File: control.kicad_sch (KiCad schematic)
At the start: 41 parts, among them J4 Conn_01x05_Pin, J5 Conn_01x03_Pin, J6 Conn_01x03_Pin, Q2 AO3400, Q3 DTC143Z, Q4 DMG1012T, SW2 SW_Push, SW3 SW_SPDT, U6 STM32G031G8Ux

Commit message: Prepeared production files
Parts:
- SW2: LCSC C2837531 -> C398057
- SW3: LCSC C398057 -> C431548
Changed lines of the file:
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@@
 			)
 		)
-		(property "LCSC" "C398057"
+		(property "LCSC" "C431548"
 			(at 260.35 38.1 0)
 			(effects
@@
 			)
 		)
-		(property "LCSC" "C2837531"
+		(property "LCSC" "C398057"
 			(at 204.47 58.42 0)
 			(effects

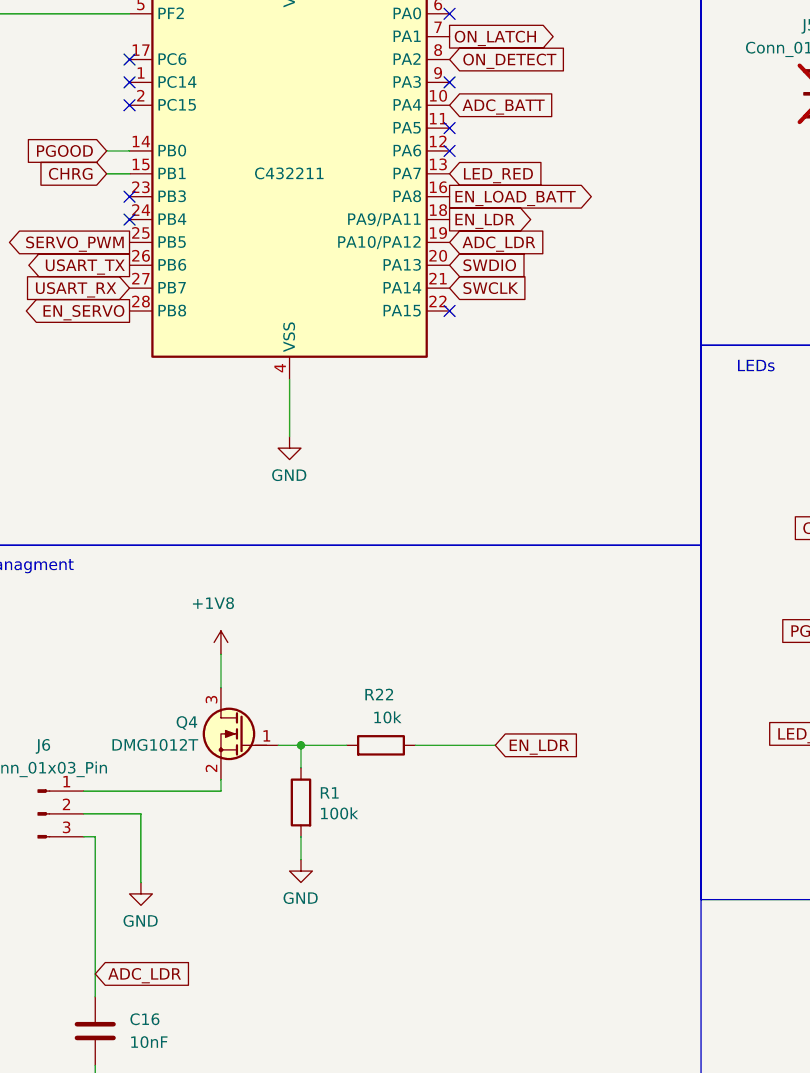
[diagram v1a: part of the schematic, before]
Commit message: Cleaned up libs
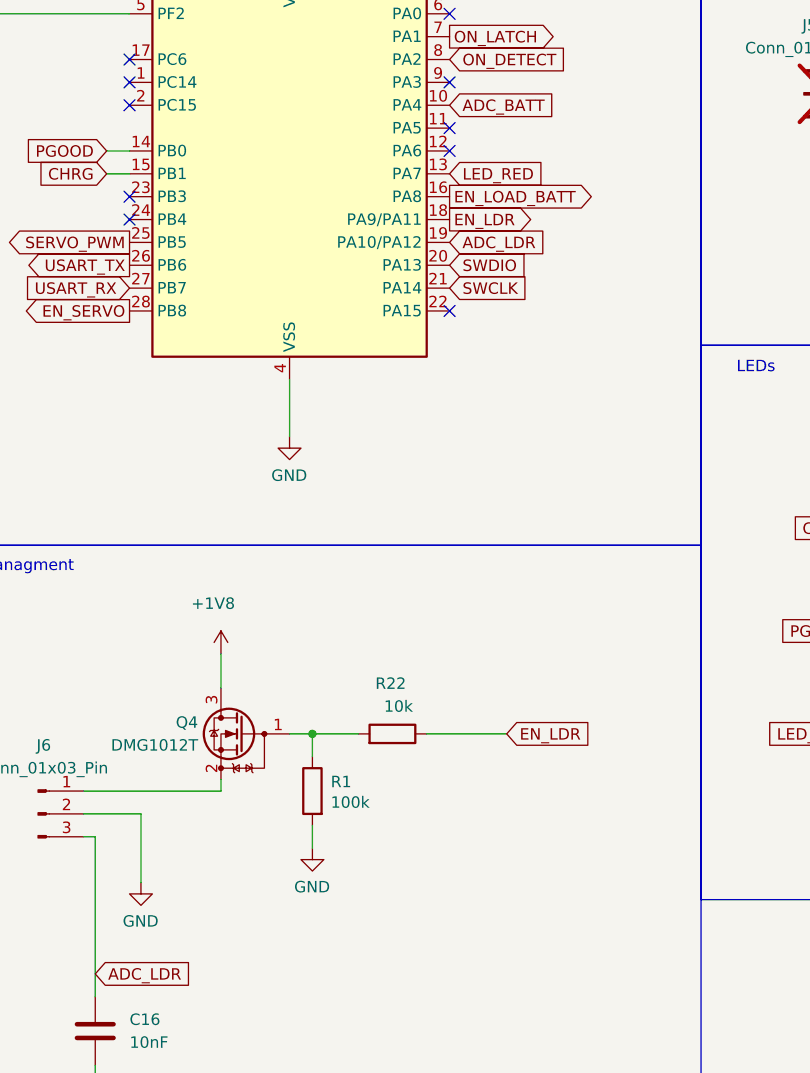
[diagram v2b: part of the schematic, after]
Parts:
- J4: footprint conn:PinHeader_1x05_P1.27mm_Vertical -> Connector_Muffin_THT.pretty:PinHeader_1x05_P1.27mm_Vertical_clear_silk
- J5: footprint conn:PinHeader_1x03_P1.27mm_Vertical -> Connector_Muffin_THT.pretty:PinHeader_1x03_P1.27mm_Vertical_clear_silk
- J6: footprint Muffin_CONNECTOR_THT:Connector_JST_1x03_P1.27mm -> Connector_Muffin_THT.pretty:Connector_JST_1x03_P1.27mm
- Q3: footprint SOT-523:SOT-523 -> Muffin_SMD:SOT-523
- Q4: symbol PCM_Transistor_MOSFET_AKL:DMG1012T -> Transistor_FET:DMG1012T
- U6: symbol stm32g031g8ux:STM32G031G8Ux -> Muffin_MCU:STM32G031G8Ux
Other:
- moved on the sheet: R1, R22
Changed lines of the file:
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@@
 	)
 	(junction
-		(at 85.09 144.78)
+		(at 86.36 143.51)
 		(diameter 0)
 		(color 0 0 0 0)
@@
 	(wire
 		(pts
-			(xy 97.79 144.78) (xy 106.68 144.78)
+			(xy 99.06 143.51) (xy 107.95 143.51)
 		)
 		(stroke
@@
 	(wire
 		(pts
-			(xy 85.09 144.78) (xy 90.17 144.78)
+			(xy 86.36 143.51) (xy 91.44 143.51)
 		)
 		(stroke
@@
 	(wire
 		(pts
-			(xy 85.09 154.94) (xy 85.09 157.48)
+			(xy 86.36 153.67) (xy 86.36 156.21)
 		)
 		(stroke
@@
 	(wire
 		(pts
-			(xy 82.55 144.78) (xy 85.09 144.78)
+			(xy 83.82 143.51) (xy 86.36 143.51)
 		)
 		(stroke
@@
 	(wire
 		(pts
-			(xy 85.09 144.78) (xy 85.09 147.32)
+			(xy 86.36 143.51) (xy 86.36 146.05)
 		)
 		(stroke
@@
 	(global_label "EN_LDR"
 		(shape input)
-		(at 106.68 144.78 0)
+		(at 107.95 143.51 0)
 		(fields_autoplaced yes)
 		(effects
@@
 		)
 		(property "Intersheetrefs" "${INTERSHEET_REFS}"
-			(at 116.6804 144.78 0)
+			(at 117.9504 143.51 0)
 			(effects
 				(font
@@
 			)
 		)
-		(property "Footprint" "conn:PinHeader_1x05_P1.27mm_Vertical"
+		(property "Footprint" "Connector_Muffin_THT.pretty:PinHeader_1x05_P1.27mm_Vertical_clear_silk"
 			(at 139.7 46.99 0)
 			(effects
@@
 	)
 	(symbol
-		(lib_id "PCM_Transistor_MOSFET_AKL:DMG1012T")
+		(lib_id "Transistor_FET:DMG1012T")
 		(at 78.74 143.51 0)
 		(mirror y)
@@
 		)
 		(property "Footprint" "Muffin_SMD:SOT-523"
-			(at 73.66 140.97 0)
+			(at 73.66 145.415 0)
 			(effects
 				(font
 					(size 1.27 1.27)
 				)
+				(justify left)
 				(hide yes)
 			)
 		)
-		(property "Datasheet" "https://www.tme.eu/Document/41ce6a9ee591bb7bae22a8b9f76bcbce/DMG1012T-DTE.pdf"
-			(at 78.74 143.51 0)
+		(property "Datasheet" "https://www.diodes.com/assets/Datasheets/ds31783.pdf"
+			(at 73.66 147.32 0)
 			(effects
 				(font
 					(size 1.27 1.27)
 				)
+				(justify left)
 				(hide yes)
 			)
 		)
-		(property "Description" "SOT-523 N-MOSFET enchancement mode transistor, 20V, 630mA, 280mW, Alternate KiCAD Library"
+		(property "Description" "20V Vds, 0.63 Id, N-Channel MOSFET with ESD protection, SOT-523"
 			(at 78.74 143.51 0)
 			(effects
@@
 			)
 		)
-		(property "Footprint" "conn:PinHeader_1x03_P1.27mm_Vertical"
+		(property "Footprint" "Connector_Muffin_THT.pretty:PinHeader_1x03_P1.27mm_Vertical_clear_silk"
 			(at 140.97 72.39 0)
 			(effects
@@
 			)
 		)
-		(property "Footprint" "Muffin_CONNECTOR_THT:Connector_JST_1x03_P1.27mm"
+		(property "Footprint" "Connector_Muffin_THT.pretty:Connector_JST_1x03_P1.27mm"
 			(at 56.896 163.068 0)
 			(effects
@@
 			)
 		)
-		(property "Footprint" "SOT-523:SOT-523"
+		(property "Footprint" "Muffin_SMD:SOT-523"
 			(at 238.76 58.42 0)
 			(effects
@@
 	(symbol
 		(lib_id "Device:R")
-		(at 93.98 144.78 270)
+		(at 95.25 143.51 270)
 		(mirror x)
 		(unit 1)
@@
 		(dnp no)
 		(property "Reference" "R22"
-			(at 95.504 139.192 90)
+			(at 96.774 137.922 90)
 			(effects
 				(font
@@
 		)
 		(property "Value" "10k"
-			(at 96.266 141.732 90)
+			(at 97.536 140.462 90)
 			(effects
 				(font
@@
 		)
 		(property "Footprint" "Resistor_SMD:R_0603_1608Metric"
-			(at 93.98 146.558 90)
+			(at 95.25 145.288 90)
 			(effects
 				(font
@@
 		)
 		(property "Datasheet" "~"
-			(at 93.98 144.78 0)
+			(at 95.25 143.51 0)
 			(effects
 				(font
@@
 		)
 		(property "Description" "Resistor"
-			(at 93.98 144.78 0)
+			(at 95.25 143.51 0)
 			(effects
 				(font
@@
 		)
 		(property "lcsc" ""
-			(at 93.98 144.78 0)
+			(at 95.25 143.51 0)
 			(effects
 				(font
@@
 		)
 		(property "Tolerance " ""
-			(at 93.98 144.78 90)
+			(at 95.25 143.51 90)
 			(effects
 				(font
@@
 	(symbol
 		(lib_id "power:GND")
-		(at 85.09 157.48 0)
+		(at 86.36 156.21 0)
 		(mirror y)
 		(unit 1)
@@
 		(dnp no)
 		(property "Reference" "#PWR029"
-			(at 85.09 163.83 0)
+			(at 86.36 162.56 0)
 			(effects
 				(font
@@
 		)
 		(property "Value" "GND"
-			(at 83.058 161.798 0)
+			(at 84.328 160.528 0)
 			(effects
 				(font
@@
 		)
 		(property "Footprint" ""
-			(at 85.09 157.48 0)
+			(at 86.36 156.21 0)
 			(effects
 				(font
@@
 		)
 		(property "Datasheet" ""
-			(at 85.09 157.48 0)
+			(at 86.36 156.21 0)
 			(effects
 				(font
@@
 		)
 		(property "Description" "Power symbol creates a global label with name \"GND\" , ground"
-			(at 85.09 157.48 0)
+			(at 86.36 156.21 0)
 			(effects
 				(font
@@
 	)
 	(symbol
-		(lib_id "stm32g031g8ux:STM32G031G8Ux")
+		(lib_id "Muffin_MCU:STM32G031G8Ux")
 		(at 83.82 81.28 0)
 		(unit 1)
@@
 					(size 1.27 1.27)
 				)
+				(hide yes)
 			)
 		)
@@
 	(symbol
 		(lib_id "Device:R")
-		(at 85.09 151.13 0)
+		(at 86.36 149.86 0)
 		(mirror y)
 		(unit 1)
@@
 		(dnp no)
 		(property "Reference" "R1"
-			(at 87.122 150.114 0)
+			(at 88.392 148.844 0)
 			(effects
 				(font
@@
 		)
 		(property "Value" "100k"
-			(at 87.122 152.4 0)
+			(at 88.392 151.13 0)
 			(effects
 				(font
@@
 		)
 		(property "Footprint" "Resistor_SMD:R_0603_1608Metric"
-			(at 86.868 151.13 90)
+			(at 88.138 149.86 90)
 			(effects
 				(font
@@
 		)
 		(property "Datasheet" "~"
-			(at 85.09 151.13 0)
+			(at 86.36 149.86 0)
 			(effects
 				(font
@@
 		)
 		(property "Description" "Resistor"
-			(at 85.09 151.13 0)
+			(at 86.36 149.86 0)
 			(effects
 				(font
@@
 		)
 		(property "lcsc" ""
-			(at 85.09 151.13 0)
+			(at 86.36 149.86 0)
 			(effects
 				(font
@@
 		)
 		(property "Tolerance " ""
-			(at 85.09 151.13 0)
+			(at 86.36 149.86 0)
 			(effects
 				(font

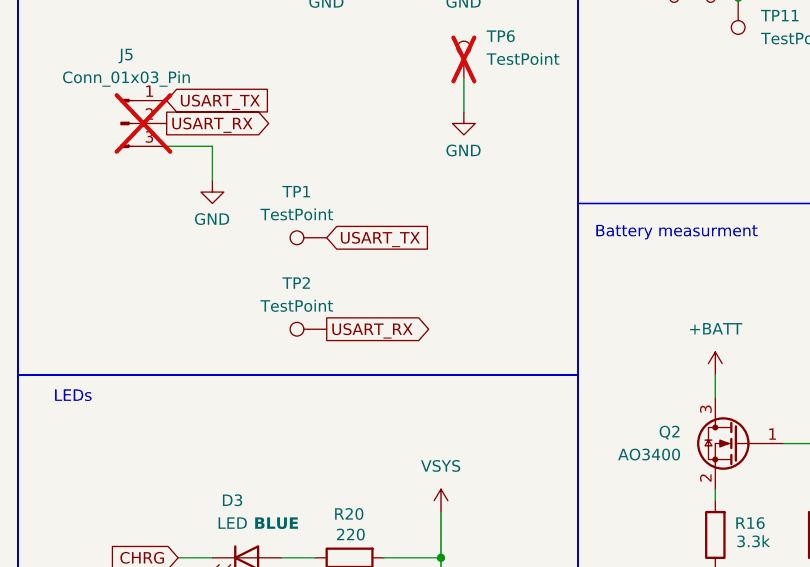
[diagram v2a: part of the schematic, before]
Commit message: Updated project jobset - Added generation of ibom - Updated production files
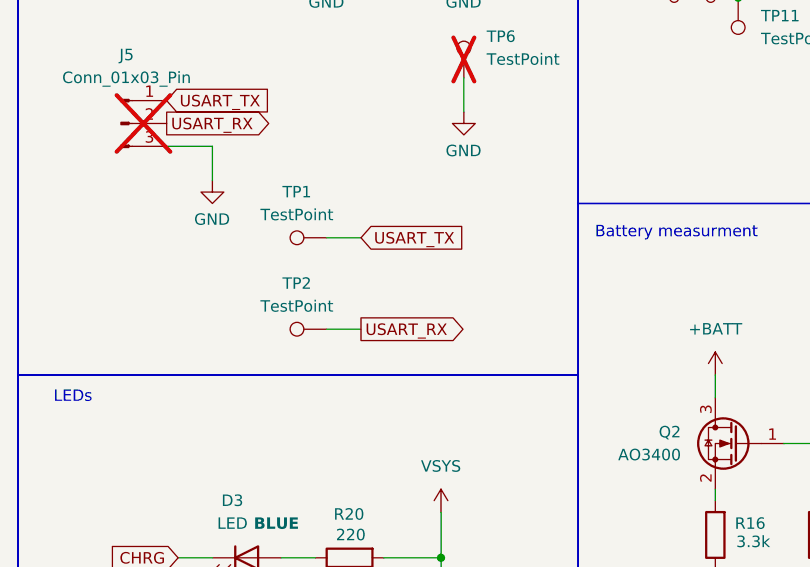
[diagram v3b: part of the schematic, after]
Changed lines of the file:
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@@
 	(wire
 		(pts
+			(xy 167.64 95.25) (xy 163.83 95.25)
+		)
+		(stroke
+			(width 0)
+			(type default)
+		)
+	)
+	(wire
+		(pts
 			(xy 147.32 143.51) (xy 151.13 143.51)
 		)
@@
 	(wire
 		(pts
+			(xy 167.64 85.09) (xy 163.83 85.09)
+		)
+		(stroke
+			(width 0)
+			(type default)
+		)
+	)
+	(wire
+		(pts
 			(xy 218.44 121.92) (xy 218.44 123.19)
 		)
@@
 	(global_label "USART_TX"
 		(shape input)
-		(at 163.83 85.09 0)
+		(at 167.64 85.09 0)
 		(fields_autoplaced yes)
 		(effects
@@
 		)
 		(property "Intersheetrefs" "${INTERSHEET_REFS}"
-			(at 175.8261 85.09 0)
+			(at 179.6361 85.09 0)
 			(effects
 				(font
@@
 		)
 		(property "Netclass" "DATA"
-			(at 163.83 87.2808 0)
+			(at 167.64 87.2808 0)
 			(effects
 				(font
@@
 	(global_label "USART_RX"
 		(shape output)
-		(at 163.83 95.25 0)
+		(at 167.64 95.25 0)
 		(fields_autoplaced yes)
 		(effects
@@
 		)
 		(property "Intersheetrefs" "${INTERSHEET_REFS}"
-			(at 176.1285 95.25 0)
+			(at 179.9385 95.25 0)
 			(effects
 				(font
@@
 		)
 		(property "Netclass" "DATA"
-			(at 163.83 97.4408 0)
+			(at 167.64 97.4408 0)
 			(effects
 				(font
@@
 			)
 		)
-		(property "lcsc" ""
-			(at 209.55 107.95 0)
-			(effects
-				(font
-					(size 1.27 1.27)
-				)
-			)
-		)

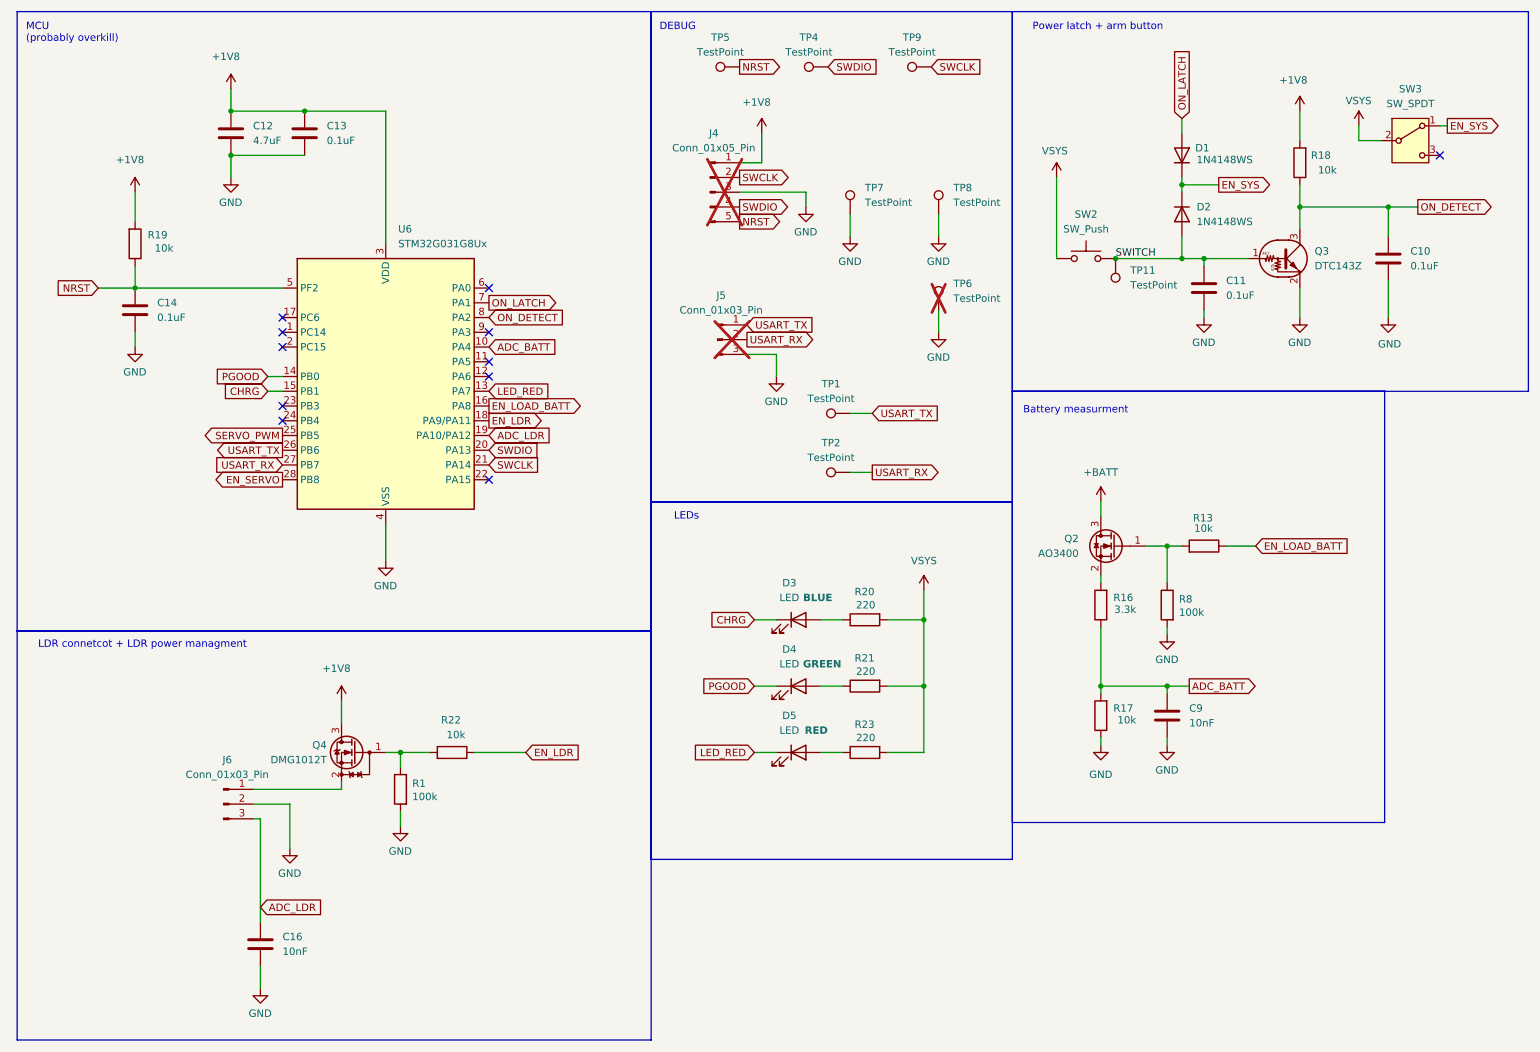
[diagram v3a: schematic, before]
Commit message: V4 revision - Moved usb to HID side - Changed battery connector to ph2.0 with standard(ish) pinout - Better footprints for debug and ldr connectors - Changed switch from SK12D07 to MSK12C02 - Changed R(ILIM) to 1.1k - Better placement of servo power and connector - Changed thermistor to 0402 SMD - Removed jumper to NTC
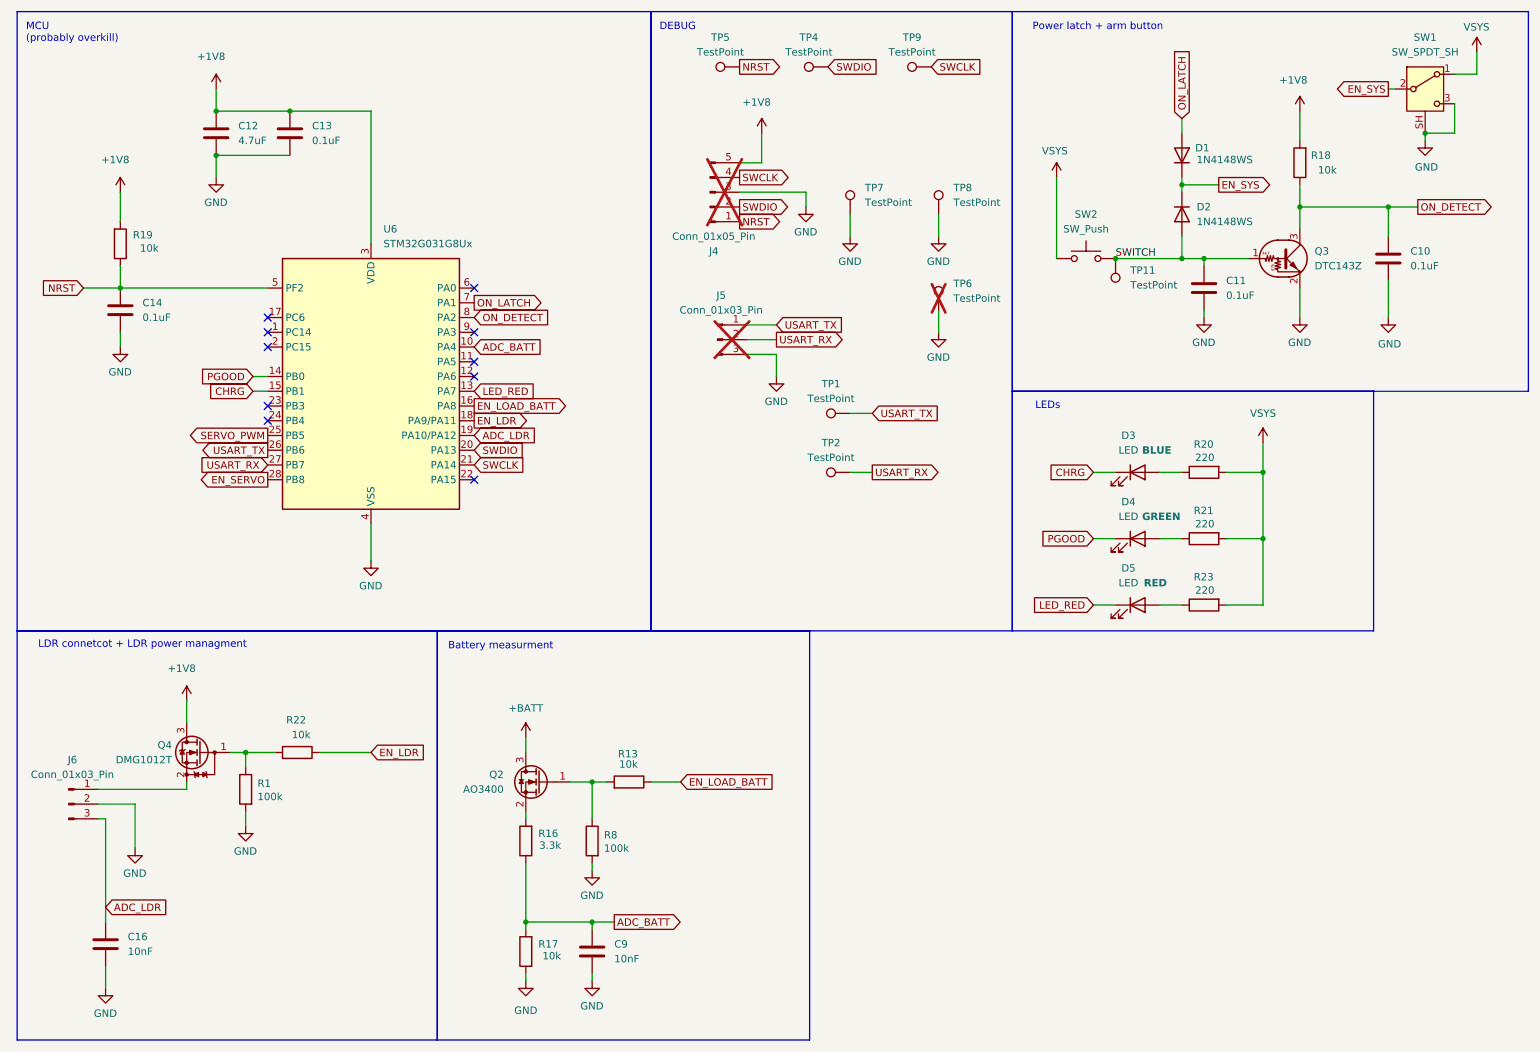
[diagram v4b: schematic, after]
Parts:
- removed SW3: SW_SPDT, Button_Switch_THT:SW_Slide_SPDT_Angled_CK_OS102011MA1Q, symbol Switch:SW_SPDT
- added SW1: SW_SPDT_SH, Muffin_SMD:MSK12C02, symbol Muffin_SWITCH:SW_SPDT_SH
- J4: footprint Connector_Muffin_THT.pretty:PinHeader_1x05_P1.27mm_Vertical_clear_silk -> Connector_Muffin_THT.pretty:Molex_PicoBlade_53048-0510_1x05_P1.25mm_Horizontal
- J5: footprint Connector_Muffin_THT.pretty:PinHeader_1x03_P1.27mm_Vertical_clear_silk -> Connector_Muffin_THT.pretty:Molex_PicoBlade_53048-0310_1x03_P1.25mm_Horizontal
- J6: footprint Connector_Muffin_THT.pretty:Connector_JST_1x03_P1.27mm -> Connector_Muffin_THT.pretty:Molex_PicoBlade_53048-0310_1x03_P1.25mm_Horizontal
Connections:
- net +1V8: now also J4.5 (Pin_5); no longer J4.1 (Pin_1)
- net EN_SYS: now also SW1.2 (B)
- net GND: now also SW1.3 (C), SW1.SH (Shield)
- net NRST: now also J4.1 (Pin_1); no longer J4.5 (Pin_5)
- net SWCLK: now also J4.4 (Pin_4); no longer J4.2 (Pin_2)
- net SWDIO: now also J4.2 (Pin_2); no longer J4.4 (Pin_4)
- net VSYS: now also SW1.1 (A)
- no-connect marks 11 -> 10
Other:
- moved on the sheet: C12, C13, C14, C16, C9, D3, D4, D5, J6, Q2, Q4, R1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

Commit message: v4.1 - Changed SW2 to SMT (with lower profile) - Widen annular ring of vias - Small changes in routing (due to wider vias)
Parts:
- C16, C9: value 10nF -> 1nF
- R20, R21, R23: value 220 -> 1.1k
- SW2: footprint Button_Switch_THT:SW_Tactile_SPST_Angled_PTS645Vx58-2LFS -> Button_Switch_SMD:SW_SPST_EVQP7C
- TP6: footprint TestPoint:TestPoint_Plated_Hole_D2.0mm -> TestPoint:TestPoint_Plated_Hole_D4.0mm
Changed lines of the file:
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@@
 			)
 		)
-		(property "Value" "10nF"
+		(property "Value" "1nF"
 			(at 39.37 177.7999 0)
 			(effects
@@
 			)
 		)
-		(property "Value" "220"
+		(property "Value" "1.1k"
 			(at 223.266 115.57 90)
 			(effects
@@
 		(on_board yes)
 		(dnp yes)
-		(fields_autoplaced yes)
 		(property "Reference" "J5"
 			(at 141.605 64.77 0)
@@
 			)
 		)
-		(property "Value" "220"
+		(property "Value" "1.1k"
 			(at 223.266 92.71 90)
 			(effects
@@
 			)
 		)
-		(property "Value" "10nF"
+		(property "Value" "1nF"
 			(at 123.19 179.0699 0)
 			(effects
@@
 			)
 		)
-		(property "Value" "220"
+		(property "Value" "1.1k"
 			(at 223.266 104.14 90)
 			(effects
@@
 			)
 		)
-		(property "Footprint" "Button_Switch_THT:SW_Tactile_SPST_Angled_PTS645Vx58-2LFS"
+		(property "Footprint" "Button_Switch_SMD:SW_SPST_EVQP7C"
 			(at 204.47 53.34 0)
 			(effects
@@
 			)
 		)
-		(property "Footprint" "TestPoint:TestPoint_Plated_Hole_D2.0mm"
+		(property "Footprint" "TestPoint:TestPoint_Plated_Hole_D4.0mm"
 			(at 184.15 67.31 0)
 			(effects
